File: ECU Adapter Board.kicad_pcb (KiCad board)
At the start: 2 copper layers, 150 x 100 mm, 28 parts, among them J1 Conn_01x03_Pin, J11 Conn_01x03_Pin, J13 Conn_01x03_Pin, J15 Conn_01x03_Pin, J17 Conn_01x03_Pin, J18 DSUB_15pin/VGA Veritical Fema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, J19 Conn_01x03_Pin, J2 DSUB_15pin/VGA Veritical Fema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, J20 DSUB_15pin/VGA Veritical Fema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, J21 Conn_01x03_Pin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

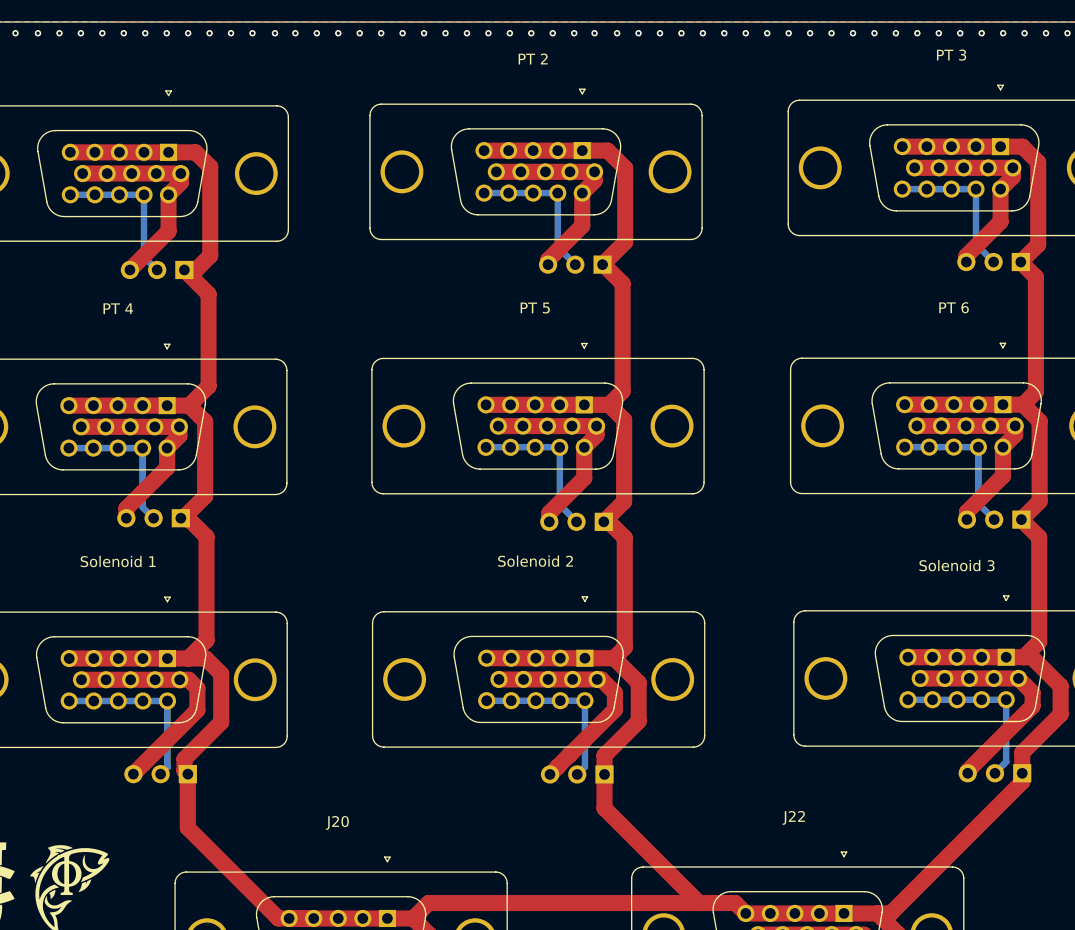
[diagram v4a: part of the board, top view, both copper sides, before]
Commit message: added UCIRP repo submodule, fixed silkscreen
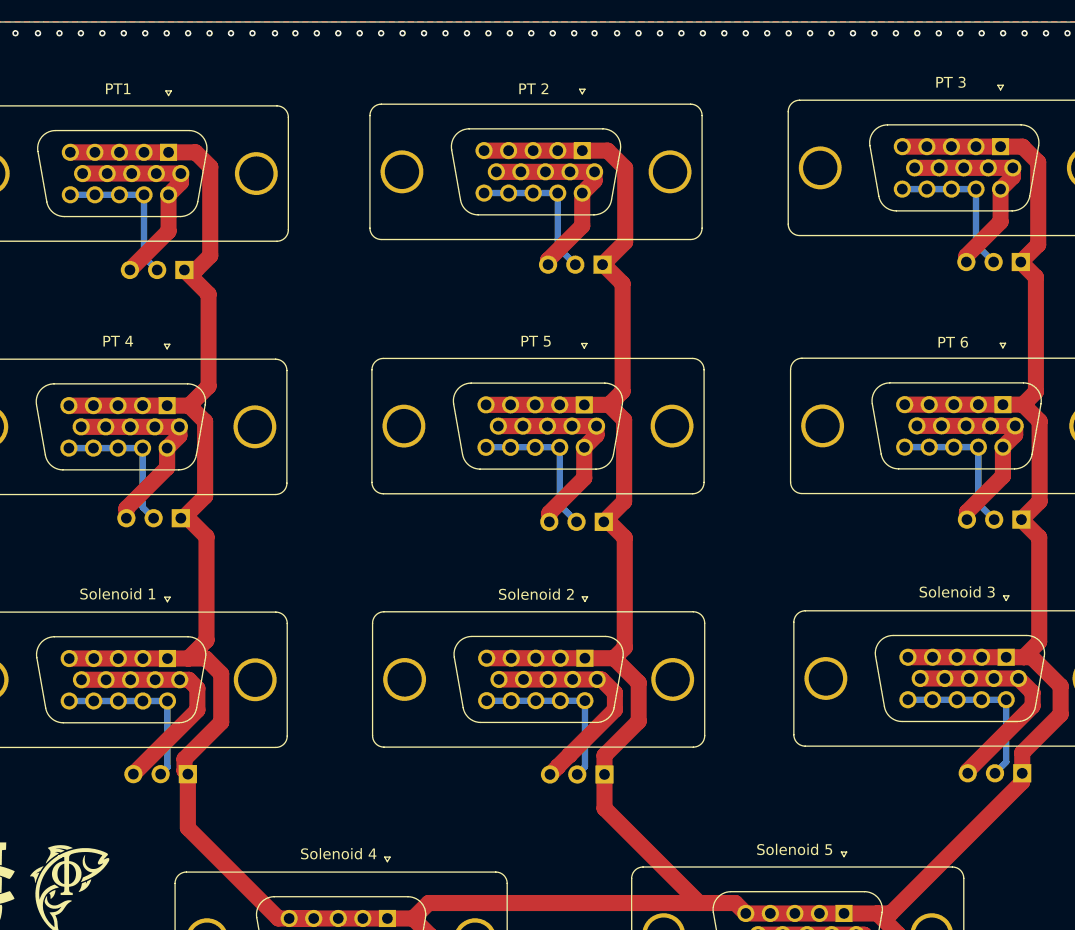
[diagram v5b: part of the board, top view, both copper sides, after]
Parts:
- Solenoid 4: renamed from J20
- Solenoid 5: renamed from J22
- renumbered J2 to PT1
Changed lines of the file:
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@@
 		(at 193.085 53.595)
 		(property "Reference" "PT 5"
-			(at 0 -0.5 0)
+			(at 0.085 2.595 0)
 			(unlocked yes)
 			(layer "F.SilkS")
@@
 		)
 		(embedded_fonts no)
+		(model "${KICAD9_3DMODEL_DIR}/Connector_Dsub.3dshapes/DSUB-15-HD_Socket_Vertical_P2.29x1.98mm_MountingHoles.step"
+			(offset
+				(xyz 4.5 -8.5 0)
+			)
+			(scale
+				(xyz 1 1 1)
+			)
+			(rotate
+				(xyz -0 -0 -0)
+			)
+		)
 	)
 	(footprint "UCIRP-KiCAD-Lib:Connector_VGA_Vertical"
@@
 		(at 231.905 29.515)
 		(property "Reference" "PT 3"
-			(at 0 0 0)
+			(at -0.055 2.535 0)
 			(unlocked yes)
 			(layer "F.SilkS")
@@
 		)
 		(embedded_fonts no)
+		(model "${KICAD9_3DMODEL_DIR}/Connector_Dsub.3dshapes/DSUB-15-HD_Socket_Vertical_P2.29x1.98mm_MountingHoles.step"
+			(offset
+				(xyz 4.5 -8.5 0)
+			)
+			(scale
+				(xyz 1 1 1)
+			)
+			(rotate
+				(xyz -0 -0 -0)
+			)
+		)
 	)
 	(footprint "UCIRP-KiCAD-Lib:Connector_VGA_Vertical"
 		(layer "F.Cu")
 		(at 217.305 101.02)
-		(property "Reference" "J22"
-			(at 0 -0.5 0)
+		(property "Reference" "Solenoid 5"
+			(at -0.005 2.58 0)
 			(unlocked yes)
 			(layer "F.SilkS")
@@
 		)
 		(embedded_fonts no)
+		(model "${KICAD9_3DMODEL_DIR}/Connector_Dsub.3dshapes/DSUB-15-HD_Socket_Vertical_P2.29x1.98mm_MountingHoles.step"
+			(offset
+				(xyz 4.5 -8.5 0)
+			)
+			(scale
+				(xyz 1 1 1)
+			)
+			(rotate
+				(xyz -0 -0 -0)
+			)
+		)
 	)
 	(footprint "UCIRP-KiCAD-Lib:Connector_VGA_Vertical"
 		(layer "F.Cu")
 		(at 154.32 30.045)
-		(property "Reference" "J2"
-			(at 0 -0.5 0)
+		(property "Reference" "PT1"
+			(at -0.12 2.615 0)
 			(unlocked yes)
 			(layer "F.SilkS")
-			(hide yes)
 			(effects
 				(font
@@
 		)
 		(embedded_fonts no)
+		(model "${KICAD9_3DMODEL_DIR}/Connector_Dsub.3dshapes/DSUB-15-HD_Socket_Vertical_P2.29x1.98mm_MountingHoles.step"
+			(offset
+				(xyz 4.5 -8.5 0)
+			)
+			(scale
+				(xyz 1 1 1)
+			)
+			(rotate
+				(xyz -0 -0 -0)
+			)
+		)
 	)
 	(footprint "UCIRP-KiCAD-Lib:Connector_VGA_Vertical"
@@
 		(at 154.185 53.665)
 		(property "Reference" "PT 4"
-			(at 0 -0.5 0)
+			(at -0.005 2.525 0)
 			(unlocked yes)
 			(layer "F.SilkS")
@@
 		)
 		(embedded_fonts no)
+		(model "${KICAD9_3DMODEL_DIR}/Connector_Dsub.3dshapes/DSUB-15-HD_Socket_Vertical_P2.29x1.98mm_MountingHoles.step"
+			(offset
+				(xyz 4.5 -8.5 0)
+			)
+			(scale
+				(xyz 1 1 1)
+			)
+			(rotate
+				(xyz -0 -0 -0)
+			)
+		)
 	)
 	(footprint "MountingHole:MountingHole_4.3mm_M4_Pad_Via"
@@
 		(at 193.145 77.22)
 		(property "Reference" "Solenoid 2"
-			(at 0 -0.5 0)
+			(at 0.075 2.58 0)
 			(unlocked yes)
 			(layer "F.SilkS")
@@
 		)
 		(embedded_fonts no)
+		(model "${KICAD9_3DMODEL_DIR}/Connector_Dsub.3dshapes/DSUB-15-HD_Socket_Vertical_P2.29x1.98mm_MountingHoles.step"
+			(offset
+				(xyz 4.5 -8.5 0)
+			)
+			(scale
+				(xyz 1 1 1)
+			)
+			(rotate
+				(xyz -0 -0 -0)
+			)
+		)
 	)
 	(footprint "UCIRP-KiCAD-Lib:Connector_VGA_Vertical"
 		(layer "F.Cu")
 		(at 174.725 101.49)
-		(property "Reference" "J20"
-			(at 0 -0.5 0)
+		(property "Reference" "Solenoid 4"
+			(at 0.035 2.51 0)
 			(unlocked yes)
 			(layer "F.SilkS")
@@
 		)
 		(embedded_fonts no)
+		(model "${KICAD9_3DMODEL_DIR}/Connector_Dsub.3dshapes/DSUB-15-HD_Socket_Vertical_P2.29x1.98mm_MountingHoles.step"
+			(offset
+				(xyz 4.5 -8.5 0)
+			)
+			(scale
+				(xyz 1 1 1)
+			)
+			(rotate
+				(xyz -0 -0 -0)
+			)
+		)
 	)
 	(footprint "PCB_Logo:fish logo"
@@
 		(at 154.215 77.25)
 		(property "Reference" "Solenoid 1"
-			(at 0 -0.5 0)
+			(at -0.035 2.52 0)
 			(unlocked yes)
 			(layer "F.SilkS")
@@
 		)
 		(embedded_fonts no)
+		(model "${KICAD9_3DMODEL_DIR}/Connector_Dsub.3dshapes/DSUB-15-HD_Socket_Vertical_P2.29x1.98mm_MountingHoles.step"
+			(offset
+				(xyz 4.5 -8.5 0)
+			)
+			(scale
+				(xyz 1 1 1)
+			)
+			(rotate
+				(xyz -0 -0 -0)
+			)
+		)
 	)
 	(footprint "MountingHole:MountingHole_4.3mm_M4_Pad_Via"
@@
 		)
 		(embedded_fonts no)
+		(model "${KICAD9_3DMODEL_DIR}/Connector_Dsub.3dshapes/DSUB-15-HD_Socket_Vertical_P2.29x1.98mm_MountingHoles.step"
+			(offset
+				(xyz 4.5 -8.5 0)
+			)
+			(scale
+				(xyz 1 1 1)
+			)
+			(rotate
+				(xyz -0 -0 -0)
+			)
+		)
 	)
 	(footprint "UCIRP-KiCAD-Lib:Connector_VGA_Vertical"
@@
 		(at 192.9 29.885)
 		(property "Reference" "PT 2"
-			(at 0 0 0)
+			(at 0.06 2.775 0)
 			(unlocked yes)
 			(layer "F.SilkS")
@@
 		)
 		(embedded_fonts no)
+		(model "${KICAD9_3DMODEL_DIR}/Connector_Dsub.3dshapes/DSUB-15-HD_Socket_Vertical_P2.29x1.98mm_MountingHoles.step"
+			(offset
+				(xyz 4.5 -8.5 0)
+			)
+			(scale
+				(xyz 1 1 1)
+			)
+			(rotate
+				(xyz -0 -0 -0)
+			)
+		)
 	)
 	(footprint "PCB_Logo:UCIRPL_Logo"
@@
 		(at 232.125 53.575)
 		(property "Reference" "PT 6"
-			(at 0 -0.5 0)
+			(at -0.075 2.715 0)
 			(unlocked yes)
 			(layer "F.SilkS")
@@
 		)
 		(embedded_fonts no)
+		(model "${KICAD9_3DMODEL_DIR}/Connector_Dsub.3dshapes/DSUB-15-HD_Socket_Vertical_P2.29x1.98mm_MountingHoles.step"
+			(offset
+				(xyz 4.5 -8.5 0)
+			)
+			(scale
+				(xyz 1 1 1)
+			)
+			(rotate
+				(xyz -0 -0 -0)
+			)
+		)
 	)
 	(footprint "Connector_PinHeader_2.54mm:PinHeader_1x03_P2.54mm_Vertical"
@@
 		(embedded_fonts no)
 		(model "${KICAD9_3DMODEL_DIR}/Connector_PinHeader_2.54mm.3dshapes/PinHeader_1x03_P2.54mm_Vertical.step"
+			(hide yes)
 			(offset
 				(xyz 0 0 0)
@@
 		(embedded_fonts no)
 		(model "${KICAD9_3DMODEL_DIR}/Connector_PinHeader_2.54mm.3dshapes/PinHeader_1x03_P2.54mm_Vertical.step"
+			(hide yes)
 			(offset
 				(xyz 0 0 0)
@@
 		(embedded_fonts no)
 		(model "${KICAD9_3DMODEL_DIR}/Connector_PinHeader_2.54mm.3dshapes/PinHeader_1x03_P2.54mm_Vertical.step"
+			(hide yes)
 			(offset
 				(xyz 0 0 0)
@@
 		(embedded_fonts no)
 		(model "${KICAD9_3DMODEL_DIR}/Connector_PinHeader_2.54mm.3dshapes/PinHeader_1x03_P2.54mm_Vertical.step"
+			(hide yes)
 			(offset
 				(xyz 0 0 0)
@@
 		(embedded_fonts no)
 		(model "${KICAD9_3DMODEL_DIR}/Connector_PinHeader_2.54mm.3dshapes/PinHeader_1x03_P2.54mm_Vertical.step"
+			(hide yes)
 			(offset
 				(xyz 0 0 0)
@@
 		(embedded_fonts no)
 		(model "${KICAD9_3DMODEL_DIR}/Connector_PinHeader_2.54mm.3dshapes/PinHeader_1x03_P2.54mm_Vertical.step"
+			(hide yes)
 			(offset
 				(xyz 0 0 0)
@@
 		(embedded_fonts no)
 		(model "${KICAD9_3DMODEL_DIR}/Connector_PinHeader_2.54mm.3dshapes/PinHeader_1x03_P2.54mm_Vertical.step"
+			(hide yes)
 			(offset
 				(xyz 0 0 0)
@@
 		(embedded_fonts no)
 		(model "${KICAD9_3DMODEL_DIR}/Connector_PinHeader_2.54mm.3dshapes/PinHeader_1x03_P2.54mm_Vertical.step"
+			(hide yes)
 			(offset
 				(xyz 0 0 0)
@@
 		(embedded_fonts no)
 		(model "${KICAD9_3DMODEL_DIR}/Connector_PinHeader_2.54mm.3dshapes/PinHeader_1x03_P2.54mm_Vertical.step"
+			(hide yes)
 			(offset
 				(xyz 0 0 0)
@@
 		(embedded_fonts no)
 		(model "${KICAD9_3DMODEL_DIR}/Connector_PinHeader_2.54mm.3dshapes/PinHeader_1x03_P2.54mm_Vertical.step"
+			(hide yes)
 			(offset
 				(xyz 0 0 0)
@@
 		(embedded_fonts no)
 		(model "${KICAD9_3DMODEL_DIR}/Connector_PinHeader_2.54mm.3dshapes/PinHeader_1x03_P2.54mm_Vertical.step"
+			(hide yes)
 			(offset
 				(xyz 0 0 0)
@@
 	)
 	(gr_text "Solenoid 3"
-		(at 232.43 77.13 0)
+		(at 232.45 79.59 0)
 		(layer "F.SilkS")
 		(effects

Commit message: Ready for order
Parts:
- J10: renamed from PT 5
- J12: renamed from PT 6
- J14: renamed from Solenoid 1
- J16: renamed from Solenoid 2
- J20: renamed from Solenoid 4
- J22: renamed from Solenoid 5
- J4: renamed from PT 2
- J6: renamed from PT 3
- J8: renamed from PT 4
- renumbered PT1 to J2
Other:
- board text added: "PT1"
- board text added: "PT2"
- board text added: "PT3"
- board text added: "PT4"
- board text added: "PT5"
- board text added: "PT6"
- board text added: "Solenoid 1"
- board text added: "Solenoid 2"
- board text added: "Solenoid 4"
- board text added: "Solenoid 5"
- board text added: "UCIRPL - Avionics Maahi Vidyarthi April 2026"
- board text removed: "UCIRPL - Avionics Maahi Vidyarthi 3/30/2026"
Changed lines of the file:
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@@
 		(layer "F.Cu")
 		(at 193.085 53.595)
-		(property "Reference" "PT 5"
+		(property "Reference" "J10"
 			(at 0.085 2.595 0)
 			(unlocked yes)
 			(layer "F.SilkS")
+			(hide yes)
 			(effects
 				(font
@@
 		(layer "F.Cu")
 		(at 231.905 29.515)
-		(property "Reference" "PT 3"
+		(property "Reference" "J6"
 			(at -0.055 2.535 0)
 			(unlocked yes)
 			(layer "F.SilkS")
+			(hide yes)
 			(effects
 				(font
@@
 		(layer "F.Cu")
 		(at 217.305 101.02)
-		(property "Reference" "Solenoid 5"
+		(property "Reference" "J22"
 			(at -0.005 2.58 0)
 			(unlocked yes)
 			(layer "F.SilkS")
+			(hide yes)
 			(effects
 				(font
@@
 		(layer "F.Cu")
 		(at 154.32 30.045)
-		(property "Reference" "PT1"
+		(property "Reference" "J2"
 			(at -0.12 2.615 0)
 			(unlocked yes)
 			(layer "F.SilkS")
+			(hide yes)
 			(effects
 				(font
@@
 		(layer "F.Cu")
 		(at 154.185 53.665)
-		(property "Reference" "PT 4"
+		(property "Reference" "J8"
 			(at -0.005 2.525 0)
 			(unlocked yes)
 			(layer "F.SilkS")
+			(hide yes)
 			(effects
 				(font
@@
 			(at 0 -5.25 0)
 			(layer "F.SilkS")
+			(hide yes)
 			(effects
 				(font
@@
 			)
 		)
-		(property "Datasheet" ""
+		(property "Datasheet" "~"
 			(at 0 0 0)
 			(layer "F.Fab")
@@
 			(at 0 -5.25 0)
 			(layer "F.SilkS")
+			(hide yes)
 			(effects
 				(font
@@
 			)
 		)
-		(property "Datasheet" ""
+		(property "Datasheet" "~"
 			(at 0 0 0)
 			(layer "F.Fab")
@@
 			(at 0 -5.25 0)
 			(layer "F.SilkS")
+			(hide yes)
 			(effects
 				(font
@@
 			)
 		)
-		(property "Datasheet" ""
+		(property "Datasheet" "~"
 			(at 0 0 0)
 			(layer "F.Fab")
@@
 		(layer "F.Cu")
 		(at 193.145 77.22)
-		(property "Reference" "Solenoid 2"
+		(property "Reference" "J16"
 			(at 0.075 2.58 0)
 			(unlocked yes)
 			(layer "F.SilkS")
+			(hide yes)
 			(effects
 				(font
@@
 		(layer "F.Cu")
 		(at 174.725 101.49)
-		(property "Reference" "Solenoid 4"
+		(property "Reference" "J20"
 			(at 0.035 2.51 0)
 			(unlocked yes)
 			(layer "F.SilkS")
+			(hide yes)
 			(effects
 				(font
@@
 		(layer "F.Cu")
 		(at 154.215 77.25)
-		(property "Reference" "Solenoid 1"
+		(property "Reference" "J14"
 			(at -0.035 2.52 0)
 			(unlocked yes)
 			(layer "F.SilkS")
+			(hide yes)
 			(effects
 				(font
@@
 			(at 0 -5.25 0)
 			(layer "F.SilkS")
+			(hide yes)
 			(effects
 				(font
@@
 			)
 		)
-		(property "Datasheet" ""
+		(property "Datasheet" "~"
 			(at 0 0 0)
 			(layer "F.Fab")
@@
 		(layer "F.Cu")
 		(at 192.9 29.885)
-		(property "Reference" "PT 2"
+		(property "Reference" "J4"
 			(at 0.06 2.775 0)
 			(unlocked yes)
 			(layer "F.SilkS")
+			(hide yes)
 			(effects
 				(font
@@
 		(layer "F.Cu")
 		(at 232.125 53.575)
-		(property "Reference" "PT 6"
+		(property "Reference" "J12"
 			(at -0.075 2.715 0)
 			(unlocked yes)
 			(layer "F.SilkS")
+			(hide yes)
 			(effects
 				(font
@@
 			)
 		)
-		(property "Datasheet" ""
+		(property "Datasheet" "~"
 			(at 0 0 90)
 			(layer "B.Fab")
@@
 			)
 		)
-		(property "Datasheet" ""
+		(property "Datasheet" "~"
 			(at 0 0 90)
 			(layer "B.Fab")
@@
 			)
 		)
-		(property "Datasheet" ""
+		(property "Datasheet" "~"
 			(at 0 0 90)
 			(layer "B.Fab")
@@
 			)
 		)
-		(property "Datasheet" ""
+		(property "Datasheet" "~"
 			(at 0 0 90)
 			(layer "B.Fab")
@@
 			)
 		)
-		(property "Datasheet" ""
+		(property "Datasheet" "~"
 			(at 0 0 90)
 			(layer "B.Fab")
@@
 			)
 		)
-		(property "Datasheet" ""
+		(property "Datasheet" "~"
 			(at 0 0 90)
 			(layer "B.Fab")
@@
 			)
 		)
-		(property "Datasheet" ""
+		(property "Datasheet" "~"
 			(at 0 0 90)
 			(layer "B.Fab")
@@
 			)
 		)
-		(property "Datasheet" ""
+		(property "Datasheet" "~"
 			(at 0 0 90)
 			(layer "B.Fab")
@@
 			)
 		)
-		(property "Datasheet" ""
+		(property "Datasheet" "~"
 			(at 0 0 90)
 			(layer "B.Fab")
@@
 			)
 		)
-		(property "Datasheet" ""
+		(property "Datasheet" "~"
 			(at 0 0 90)
 			(layer "B.Fab")
@@
 			)
 		)
-		(property "Datasheet" ""
+		(property "Datasheet" "~"
 			(at 0 0 90)
 			(layer "B.Fab")
@@
 		)
 	)
+	(gr_line
+		(start 118.659995 36.4)
+		(end 118.67 116.3)
+		(stroke
+			(width 0.1)
+			(type default)
+		)
+		(layer "Edge.Cuts")
+	)
 	(gr_arc
-		(start 268.67 116.4)
-		(mid 265.810843 123.401414)
-		(end 258.868 126.4)
+		(start 118.659995 36.4)
+		(mid 121.588323 29.325394)
+		(end 128.66 26.39)
 		(stroke
 			(width 0.1)
@@
 	)
 	(gr_arc
-		(start 259.041025 26.404655)
-		(mid 265.86835 29.463304)
-		(end 268.670124 36.4)
+		(start 128.77 126.4)
+		(mid 121.598576 123.471422)
+		(end 118.67 116.3)
 		(stroke
 			(width 0.1)
@@
 	)
 	(gr_arc
-		(start 128.77 126.4)
-		(mid 121.598576 123.471422)
-		(end 118.67 116.3)
+		(start 259.041025 26.404655)
+		(mid 265.86835 29.463304)
+		(end 268.670124 36.4)
 		(stroke
 			(width 0.1)
@@
 	)
 	(gr_arc
-		(start 118.659995 36.4)
-		(mid 121.588323 29.325394)
-		(end 128.66 26.39)
+		(start 268.67 116.4)
+		(mid 265.810843 123.401414)
+		(end 258.868 126.4)
 		(stroke
 			(width 0.1)
@@
 		(layer "Edge.Cuts")
 	)
-	(gr_line
-		(start 118.659995 36.4)
-		(end 118.67 116.3)
-		(stroke
-			(width 0.1)
-			(type default)
+	(gr_text "Solenoid 1"
+		(at 154.25 79.75 0)
+		(layer "F.SilkS")
+		(effects
+			(font
+				(size 1 1)
+				(thickness 0.1)
+			)
+		)
+	)
+	(gr_text "Solenoid 4"
+		(at 174.75 103.75 0)
+		(layer "F.SilkS")
+		(effects
+			(font
+				(size 1 1)
+				(thickness 0.1)
+			)
+		)
+	)
+	(gr_text "Solenoid 2"
+		(at 193.25 79.75 0)
+		(layer "F.SilkS")
+		(effects
+			(font
+				(size 1 1)
+				(thickness 0.1)
+			)
+		)
+	)
+	(gr_text "Solenoid 5"
+		(at 217.5 103.5 0)
+		(layer "F.SilkS")
+		(effects
+			(font
+				(size 1 1)
+				(thickness 0.1)
+			)
 		)
-		(layer "Edge.Cuts")
 	)
 	(gr_text "Solenoid 3"
@@
 		)
 	)
-	(gr_text "UCIRPL - Avionics\nMaahi Vidyarthi \n3/30/2026\n"
+	(gr_text "PT1"
+		(at 153.5 33.5 0)
+		(layer "F.SilkS")
+		(effects
+			(font
+				(size 1 1)
+				(thickness 0.15)
+			)
+			(justify left bottom)
+		)
+	)
+	(gr_text "PT4"
+		(at 153.5 57 0)
+		(layer "F.SilkS")
+		(effects
+			(font
+				(size 1 1)
+				(thickness 0.15)
+			)
+			(justify left bottom)
+		)
+	)
+	(gr_text "PT2"
+		(at 192 33.5 0)
+		(layer "F.SilkS")
+		(effects
+			(font
+				(size 1 1)
+				(thickness 0.15)
+			)
+			(justify left bottom)
+		)
+	)
+	(gr_text "PT5"
+		(at 192 57 0)
+		(layer "F.SilkS")
+		(effects
+			(font
+				(size 1 1)
+				(thickness 0.15)
+			)
+			(justify left bottom)
+		)
+	)
+	(gr_text "PT3"
+		(at 231 33 0)
+		(layer "F.SilkS")
+		(effects
+			(font
+				(size 1 1)
+				(thickness 0.15)
+			)
+			(justify left bottom)
+		)
+	)
+	(gr_text "PT6"
+		(at 231 57 0)
+		(layer "F.SilkS")
+		(effects
+			(font
+				(size 1 1)
+				(thickness 0.15)
+			)
+			(justify left bottom)
+		)
+	)
+	(gr_text "UCIRPL - Avionics\nMaahi Vidyarthi \nApril 2026"
 		(at 144.64 114.53 0)
 		(layer "F.SilkS")
